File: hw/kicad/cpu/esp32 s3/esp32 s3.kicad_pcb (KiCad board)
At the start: 2 copper layers, 45 x 45 mm, 42 parts, among them J1 TOP, J2 BUTTOM, J3 USB_B_Micro, SW1 SW_Push, U1 ESP32-S3-WROOM-1-N16R2, U2 ICM-42688-P

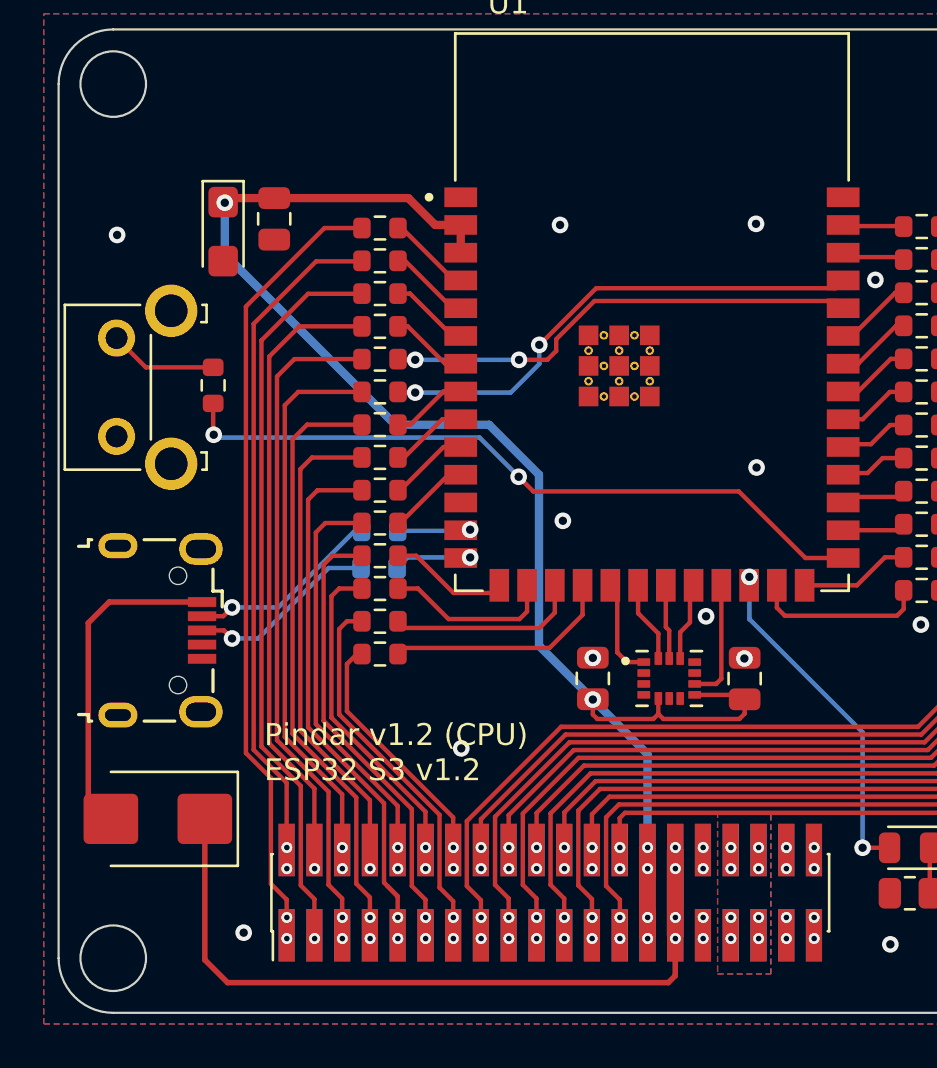
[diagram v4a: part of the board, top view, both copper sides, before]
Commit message: 更新ESP32 S3 CPU板
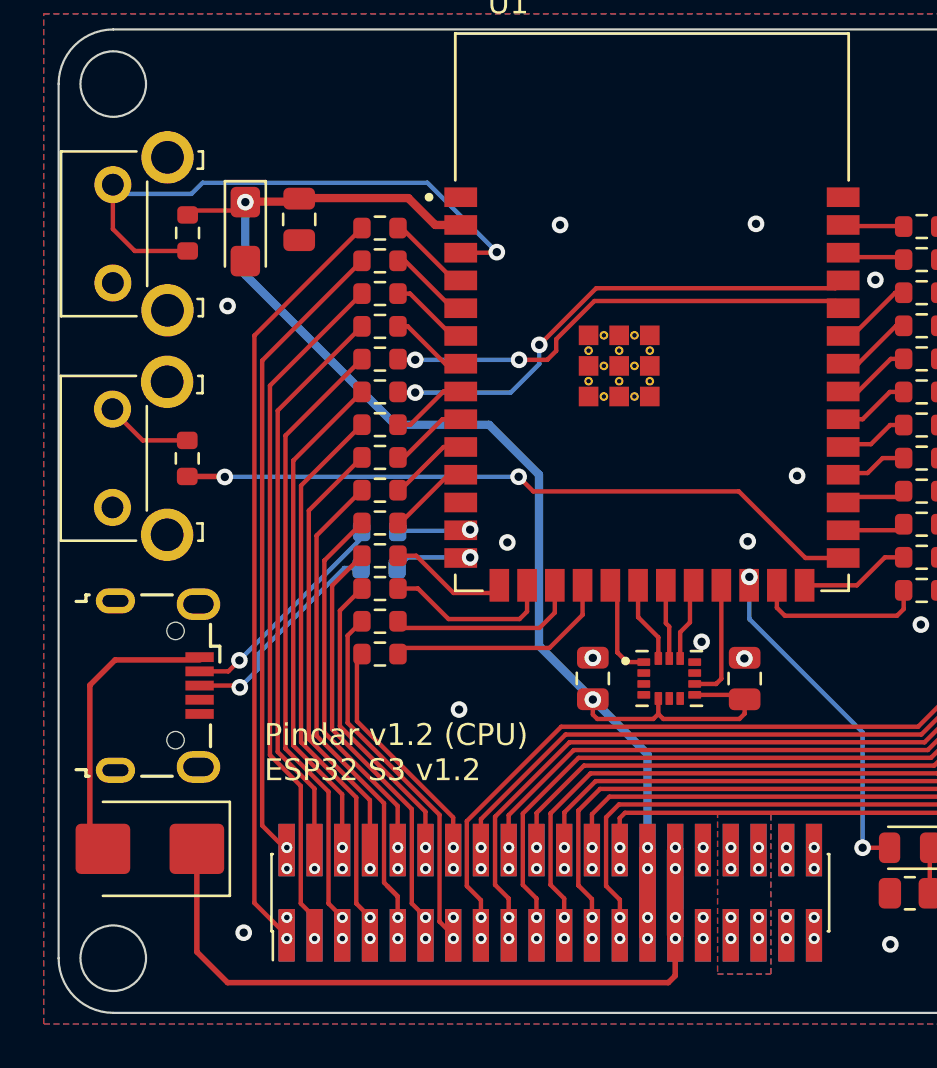
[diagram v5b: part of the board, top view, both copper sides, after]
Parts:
- added R31: 1k, Resistor_SMD:R_0603_1608Metric, F.Cu at (56.6, 42.0)
- added SW2: SW_Push, Button_Switch_THT:SW_SPST_Omron_B3F-315x_Angled, F.Cu at (53.2, 44.3)
- moved R1 3.55 mm to (56.6, 52.3)
- moved SW1 3.26 mm to (53.2, 54.6)
- moved J3 2.53 mm to (55.3, 62.7)
- moved D2 1.42 mm to (54.9, 70.2)
- moved C2 1.14 mm to (61.7, 41.4)
- moved C1 1.02 mm to (59.3, 42.0)
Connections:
- U1 pad 3: +3.3V -> Net-(U1-EN)
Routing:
- net Net-(U1-EN): track 0.00 -> 26.8 mm, vias 0 -> 1
- net /UART1_Rx: track 31.0 -> 28.9 mm
- net /UART1_Tx: track 25.2 -> 23.2 mm
- net /ADC_4: track 28.3 -> 26.3 mm
- net /UART2_Rx: track 27.6 -> 25.8 mm
- net /ADC_3: track 33.7 -> 31.9 mm
- net Net-(D2-A): track 15.0 -> 13.2 mm
- net /UART2_Tx: track 21.8 -> 20.1 mm
- net /ADC_2: track 30.9 -> 29.3 mm
- net /I2C_SDA: track 24.9 -> 23.4 mm
- net Net-(J3-D+): track 8.76 -> 10.2 mm
- net Net-(J3-D-): track 8.92 -> 10.3 mm
- net /ADC_1: track 36.3 -> 35.0 mm
- net /I2C_CLK: track 18.4 -> 17.1 mm
- net +5V: track 38.2 -> 37.0 mm
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
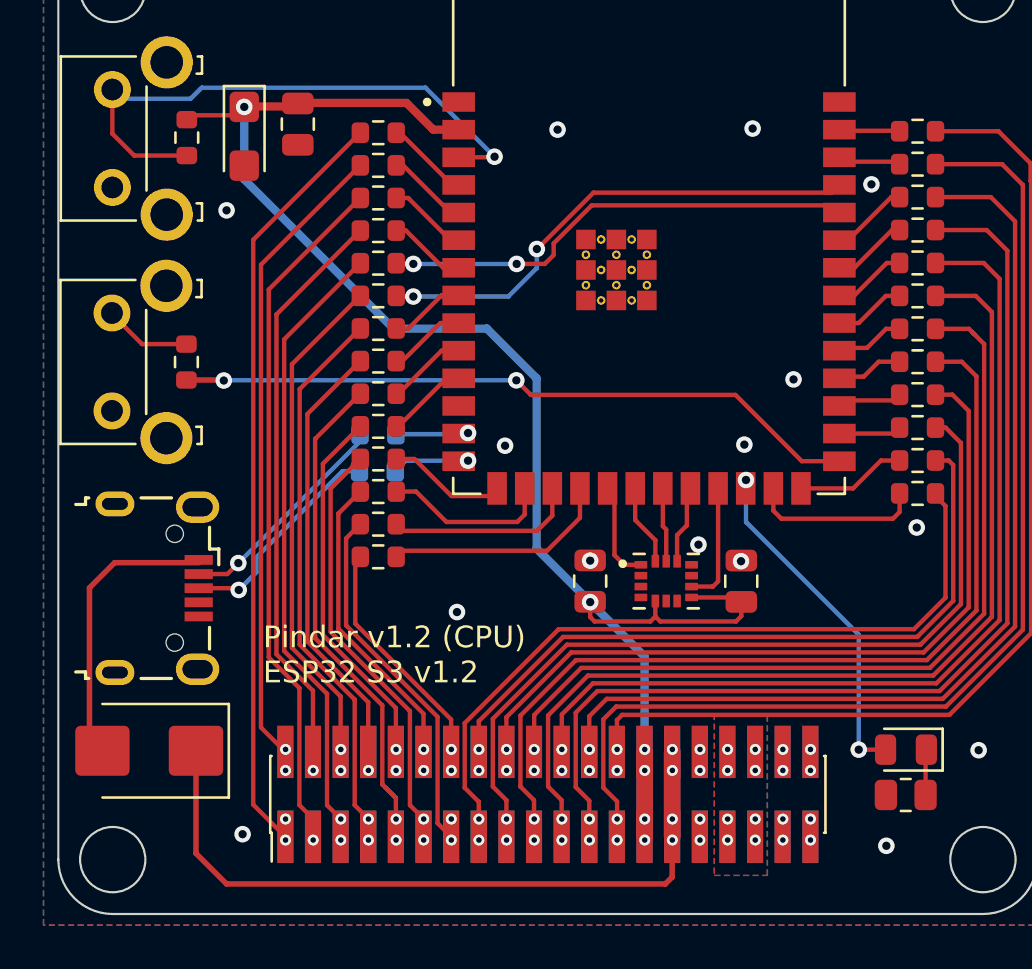
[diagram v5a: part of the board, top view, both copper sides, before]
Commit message: 更新ESP32 S3 CPU板
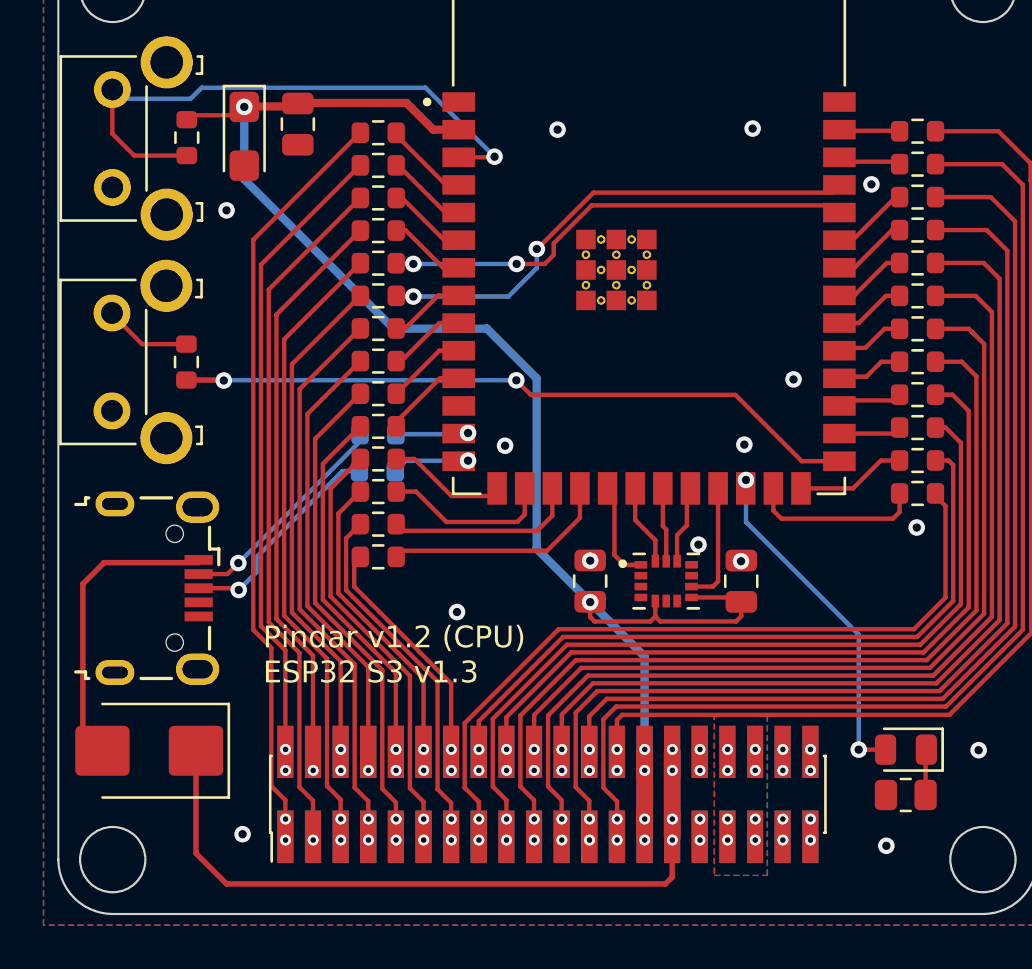
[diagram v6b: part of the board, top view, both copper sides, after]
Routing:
- net /I2C_SDA: track 23.4 -> 22.8 mm
- net Net-(D2-A): track 13.2 -> 13.8 mm
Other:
- board text added: "Pindar v1.2 (CPU) ESP32 S3 v1.3"
- board text removed: "Pindar v1.2 (CPU) ESP32 S3 v1.2"

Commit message: 更新USB micro 为优信的封装
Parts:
- J3: footprint Connector_USB:USB_Micro-B_Wuerth_629105150521 -> USB_Micro-B_YouCee:USB_Micro-B_YouCee
- moved J3 0.29 mm to (55.6, 62.7)
- moved R31 0.19 mm to (56.6, 42.2)
- moved SW2 0.14 mm to (53.2, 44.5)
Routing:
- net Net-(D2-A): track 13.8 -> 17.4 mm
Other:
- board text added: "Pindar v1.2 (CPU) ESP32 S3 v1.4"
- board text removed: "Pindar v1.2 (CPU) ESP32 S3 v1.3"
